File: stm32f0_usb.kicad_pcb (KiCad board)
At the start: 2 copper layers, 41 parts, among them J1 USB_B_Mini, J2 Conn_ARM_JTAG_SWD_10, J3 Conn_01x14_Male, J4 Conn_01x14_Male, SW1 B3S-1000P, SW2 B3S-1000P, U1 STM32F042K6Tx, U2 ADP121-AUJZ33R7, U3 USBLC6-2SC6, X1 ASV-8.000MHz

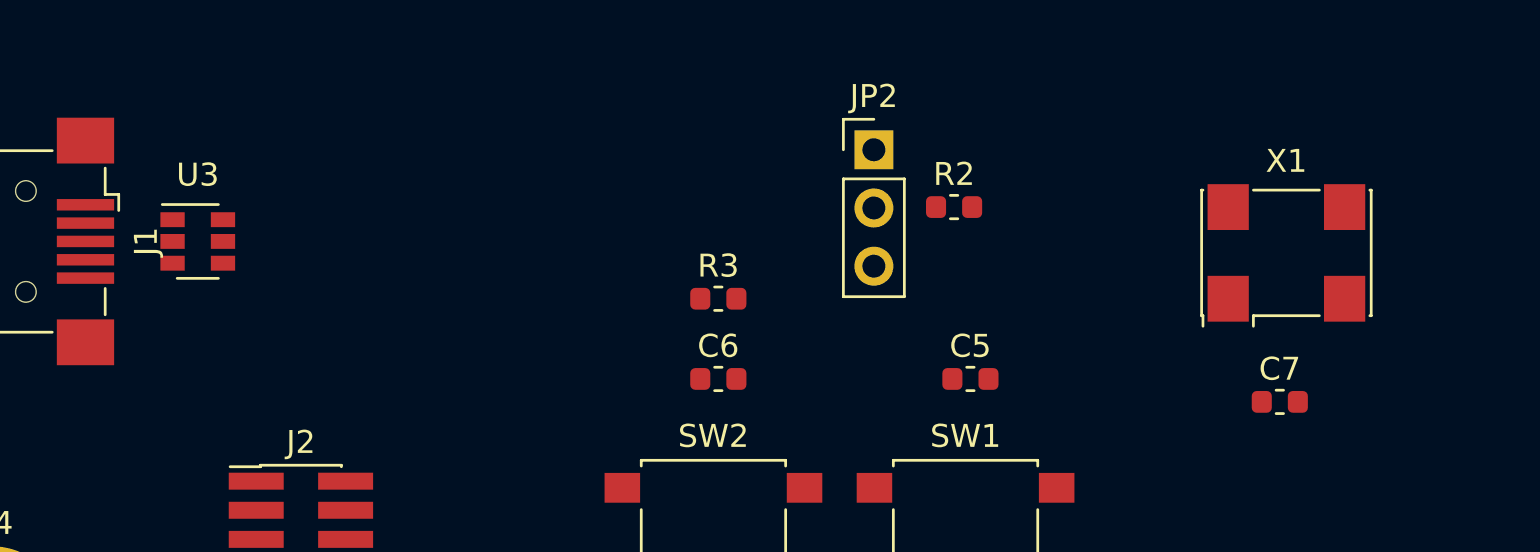
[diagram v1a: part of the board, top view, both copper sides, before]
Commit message: update usb esd connections
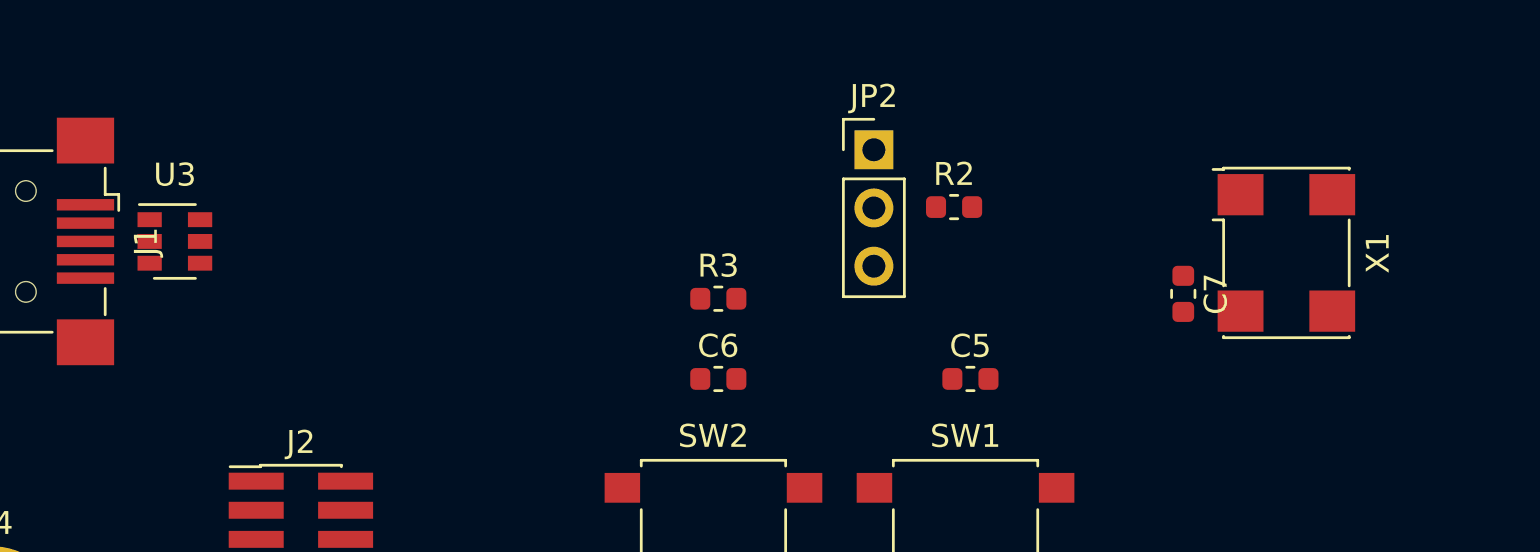
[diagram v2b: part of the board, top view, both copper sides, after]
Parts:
- moved C7 6.32 mm to (124.5, 94.8), turned to 270 degrees
- moved U3 1.00 mm to (80.5, 92.5)
- turned X1 to 270 degrees
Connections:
- D3 pad 2: /STM32/PA0 -> /STM32/PA1
- J3 pad 10: /STM32/PA7 -> /STM32/PA6
- J3 pad 11: /STM32/PA8 -> /STM32/PA7
- J3 pad 12: /STM32/PA9 -> /STM32/PB0
- J3 pad 13: /STM32/PA10 -> /STM32/PB1
- J3 pad 3: /STM32/PA0 -> /STM32/PF1
- J3 pad 4: /STM32/PA1 -> /STM32/PA0
- J3 pad 5: /STM32/PA2 -> /STM32/PA1
- J3 pad 6: /STM32/PA3 -> /STM32/PA2
- J3 pad 7: /STM32/PA4 -> /STM32/PA3
- J3 pad 8: /STM32/PA5 -> /STM32/PA4
- J3 pad 9: /STM32/PA6 -> /STM32/PA5
- J4 pad 10: /STM32/PB5 -> /STM32/PA13_SWDIO
- J4 pad 11: /STM32/PB6 -> /STM32/PA10
- J4 pad 12: /STM32/PB7 -> /STM32/PA9
- J4 pad 13: /STM32/PF1 -> /STM32/PA8
- J4 pad 3: /STM32/PA13_SWDIO -> /STM32/PB7
- J4 pad 4: /STM32/PA14_SWCLK -> /STM32/PB6
- J4 pad 5: /STM32/PA15 -> /STM32/PB5
- J4 pad 6: /STM32/PB0 -> /STM32/PB4
- J4 pad 7: /STM32/PB1 -> /STM32/PB3
- J4 pad 8: /STM32/PB3 -> /STM32/PA15
- J4 pad 9: /STM32/PB4 -> /STM32/PA14_SWCLK
- U3 pad 1: /STM32/USB_DM -> Net-(J1-Pad2)
- U3 pad 3: /STM32/USB_DP -> Net-(J1-Pad3)
- U3 pad 4: Net-(J1-Pad3) -> /STM32/USB_DP
- U3 pad 6: Net-(J1-Pad2) -> /STM32/USB_DM
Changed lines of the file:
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@@
   )
   (module Oscillator:Oscillator_SMD_Abracon_ASV-4Pin_7.0x5.1mm (layer F.Cu)
-    (at 129 93)
+    (at 129 93 270)
     (descr "Miniature Crystal Clock Oscillator Abracon ASV series, http://www.abracon.com/Oscillators/ASV.pdf, 7.0x5.1mm^2 package")
     (tags "SMD SMT crystal oscillator")
     (attr smd)
-    (fp_text reference X1 (at 0 -4) (layer F.SilkS)
-      (effects (font (size 1 1) (thickness 0.15)))
-    )
-    (fp_text value ASV-8.000MHz (at 0 4) (layer F.Fab)
+    (fp_text reference X1 (at 0 -4 90) (layer F.SilkS)
+      (effects (font (size 1 1) (thickness 0.15)))
+    )
+    (fp_text value ASV-8.000MHz (at 0 4 90) (layer F.Fab)
       (effects (font (size 1 1) (thickness 0.15)))
     )
@@
     (fp_line (start 3.4 -2.54) (end 3.5 -2.44) (layer F.Fab) (width 0.1))
     (fp_line (start -3.4 -2.54) (end 3.4 -2.54) (layer F.Fab) (width 0.1))
-    (fp_text user %R (at 0 0) (layer F.Fab)
-      (effects (font (size 1 1) (thickness 0.15)))
-    )
-    (pad 4 smd rect (at -2.54 -2) (size 1.8 2) (layers F.Cu F.Paste F.Mask)
+    (fp_text user %R (at 0 0 90) (layer F.Fab)
+      (effects (font (size 1 1) (thickness 0.15)))
+    )
+    (pad 4 smd rect (at -2.54 -2 270) (size 1.8 2) (layers F.Cu F.Paste F.Mask)
       (net 8 VDD))
-    (pad 3 smd rect (at 2.54 -2) (size 1.8 2) (layers F.Cu F.Paste F.Mask)
+    (pad 3 smd rect (at 2.54 -2 270) (size 1.8 2) (layers F.Cu F.Paste F.Mask)
       (net 47 /STM32/clkin))
-    (pad 2 smd rect (at 2.54 2) (size 1.8 2) (layers F.Cu F.Paste F.Mask)
-      (net 1 GND))
-    (pad 1 smd rect (at -2.54 2) (size 1.8 2) (layers F.Cu F.Paste F.Mask)
+    (pad 2 smd rect (at 2.54 2 270) (size 1.8 2) (layers F.Cu F.Paste F.Mask)
+      (net 1 GND))
+    (pad 1 smd rect (at -2.54 2 270) (size 1.8 2) (layers F.Cu F.Paste F.Mask)
       (net 46 "Net-(X1-Pad1)"))
     (model ${KISYS3DMOD}/Oscillator.3dshapes/Oscillator_SMD_Abracon_ASV-4Pin_7.0x5.1mm.wrl
@@
   )
   (module Package_TO_SOT_SMD:SOT-23-6 (layer F.Cu)
-    (at 81.5 92.5)
+    (at 80.5 92.5)
     (descr "6-pin SOT-23 package")
     (tags SOT-23-6)
@@
       (net 2 "Net-(C1-Pad1)"))
     (pad 6 smd rect (at 1.1 -0.95) (size 1.06 0.65) (layers F.Cu F.Paste F.Mask)
+      (net 44 /STM32/USB_DM))
+    (pad 4 smd rect (at 1.1 0.95) (size 1.06 0.65) (layers F.Cu F.Paste F.Mask)
+      (net 43 /STM32/USB_DP))
+    (pad 3 smd rect (at -1.1 0.95) (size 1.06 0.65) (layers F.Cu F.Paste F.Mask)
+      (net 15 "Net-(J1-Pad3)"))
+    (pad 2 smd rect (at -1.1 0) (size 1.06 0.65) (layers F.Cu F.Paste F.Mask)
+      (net 1 GND))
+    (pad 1 smd rect (at -1.1 -0.95) (size 1.06 0.65) (layers F.Cu F.Paste F.Mask)
       (net 16 "Net-(J1-Pad2)"))
-    (pad 4 smd rect (at 1.1 0.95) (size 1.06 0.65) (layers F.Cu F.Paste F.Mask)
-      (net 15 "Net-(J1-Pad3)"))
-    (pad 3 smd rect (at -1.1 0.95) (size 1.06 0.65) (layers F.Cu F.Paste F.Mask)
-      (net 43 /STM32/USB_DP))
-    (pad 2 smd rect (at -1.1 0) (size 1.06 0.65) (layers F.Cu F.Paste F.Mask)
-      (net 1 GND))
-    (pad 1 smd rect (at -1.1 -0.95) (size 1.06 0.65) (layers F.Cu F.Paste F.Mask)
-      (net 44 /STM32/USB_DM))
     (model ${KISYS3DMOD}/Package_TO_SOT_SMD.3dshapes/SOT-23-6.wrl
       (at (xyz 0 0 0))
@@
       (net 1 GND))
     (pad 13 thru_hole oval (at 0 30.48 90) (size 1.7 1.7) (drill 1) (layers *.Cu *.Mask)
-      (net 32 /STM32/PF1))
+      (net 24 /STM32/PA8))
     (pad 12 thru_hole oval (at 0 27.94 90) (size 1.7 1.7) (drill 1) (layers *.Cu *.Mask)
+      (net 23 /STM32/PA9))
+    (pad 11 thru_hole oval (at 0 25.4 90) (size 1.7 1.7) (drill 1) (layers *.Cu *.Mask)
+      (net 22 /STM32/PA10))
+    (pad 10 thru_hole oval (at 0 22.86 90) (size 1.7 1.7) (drill 1) (layers *.Cu *.Mask)
+      (net 21 /STM32/PA13_SWDIO))
+    (pad 9 thru_hole oval (at 0 20.32 90) (size 1.7 1.7) (drill 1) (layers *.Cu *.Mask)
+      (net 20 /STM32/PA14_SWCLK))
+    (pad 8 thru_hole oval (at 0 17.78 90) (size 1.7 1.7) (drill 1) (layers *.Cu *.Mask)
+      (net 40 /STM32/PA15))
+    (pad 7 thru_hole oval (at 0 15.24 90) (size 1.7 1.7) (drill 1) (layers *.Cu *.Mask)
+      (net 37 /STM32/PB3))
+    (pad 6 thru_hole oval (at 0 12.7 90) (size 1.7 1.7) (drill 1) (layers *.Cu *.Mask)
+      (net 36 /STM32/PB4))
+    (pad 5 thru_hole oval (at 0 10.16 90) (size 1.7 1.7) (drill 1) (layers *.Cu *.Mask)
+      (net 35 /STM32/PB5))
+    (pad 4 thru_hole oval (at 0 7.62 90) (size 1.7 1.7) (drill 1) (layers *.Cu *.Mask)
+      (net 34 /STM32/PB6))
+    (pad 3 thru_hole oval (at 0 5.08 90) (size 1.7 1.7) (drill 1) (layers *.Cu *.Mask)
       (net 33 /STM32/PB7))
-    (pad 11 thru_hole oval (at 0 25.4 90) (size 1.7 1.7) (drill 1) (layers *.Cu *.Mask)
-      (net 34 /STM32/PB6))
-    (pad 10 thru_hole oval (at 0 22.86 90) (size 1.7 1.7) (drill 1) (layers *.Cu *.Mask)
-      (net 35 /STM32/PB5))
-    (pad 9 thru_hole oval (at 0 20.32 90) (size 1.7 1.7) (drill 1) (layers *.Cu *.Mask)
-      (net 36 /STM32/PB4))
-    (pad 8 thru_hole oval (at 0 17.78 90) (size 1.7 1.7) (drill 1) (layers *.Cu *.Mask)
-      (net 37 /STM32/PB3))
-    (pad 7 thru_hole oval (at 0 15.24 90) (size 1.7 1.7) (drill 1) (layers *.Cu *.Mask)
-      (net 38 /STM32/PB1))
-    (pad 6 thru_hole oval (at 0 12.7 90) (size 1.7 1.7) (drill 1) (layers *.Cu *.Mask)
-      (net 39 /STM32/PB0))
-    (pad 5 thru_hole oval (at 0 10.16 90) (size 1.7 1.7) (drill 1) (layers *.Cu *.Mask)
-      (net 40 /STM32/PA15))
-    (pad 4 thru_hole oval (at 0 7.62 90) (size 1.7 1.7) (drill 1) (layers *.Cu *.Mask)
-      (net 20 /STM32/PA14_SWCLK))
-    (pad 3 thru_hole oval (at 0 5.08 90) (size 1.7 1.7) (drill 1) (layers *.Cu *.Mask)
-      (net 21 /STM32/PA13_SWDIO))
     (pad 2 thru_hole oval (at 0 2.54 90) (size 1.7 1.7) (drill 1) (layers *.Cu *.Mask)
       (net 1 GND))
@@
       (net 1 GND))
     (pad 13 thru_hole oval (at 0 30.48 90) (size 1.7 1.7) (drill 1) (layers *.Cu *.Mask)
-      (net 22 /STM32/PA10))
+      (net 38 /STM32/PB1))
     (pad 12 thru_hole oval (at 0 27.94 90) (size 1.7 1.7) (drill 1) (layers *.Cu *.Mask)
-      (net 23 /STM32/PA9))
+      (net 39 /STM32/PB0))
     (pad 11 thru_hole oval (at 0 25.4 90) (size 1.7 1.7) (drill 1) (layers *.Cu *.Mask)
-      (net 24 /STM32/PA8))
+      (net 25 /STM32/PA7))
     (pad 10 thru_hole oval (at 0 22.86 90) (size 1.7 1.7) (drill 1) (layers *.Cu *.Mask)
-      (net 25 /STM32/PA7))
+      (net 26 /STM32/PA6))
     (pad 9 thru_hole oval (at 0 20.32 90) (size 1.7 1.7) (drill 1) (layers *.Cu *.Mask)
-      (net 26 /STM32/PA6))
+      (net 27 /STM32/PA5))
     (pad 8 thru_hole oval (at 0 17.78 90) (size 1.7 1.7) (drill 1) (layers *.Cu *.Mask)
-      (net 27 /STM32/PA5))
+      (net 28 /STM32/PA4))
     (pad 7 thru_hole oval (at 0 15.24 90) (size 1.7 1.7) (drill 1) (layers *.Cu *.Mask)
-      (net 28 /STM32/PA4))
+      (net 29 /STM32/PA3))
     (pad 6 thru_hole oval (at 0 12.7 90) (size 1.7 1.7) (drill 1) (layers *.Cu *.Mask)
-      (net 29 /STM32/PA3))
+      (net 30 /STM32/PA2))
     (pad 5 thru_hole oval (at 0 10.16 90) (size 1.7 1.7) (drill 1) (layers *.Cu *.Mask)
-      (net 30 /STM32/PA2))
+      (net 31 /STM32/PA1))
     (pad 4 thru_hole oval (at 0 7.62 90) (size 1.7 1.7) (drill 1) (layers *.Cu *.Mask)
-      (net 31 /STM32/PA1))
+      (net 11 /STM32/PA0))
     (pad 3 thru_hole oval (at 0 5.08 90) (size 1.7 1.7) (drill 1) (layers *.Cu *.Mask)
-      (net 11 /STM32/PA0))
+      (net 32 /STM32/PF1))
     (pad 2 thru_hole oval (at 0 2.54 90) (size 1.7 1.7) (drill 1) (layers *.Cu *.Mask)
       (net 1 GND))
@@
     (fp_line (start 0.8 -0.4) (end -0.5 -0.4) (layer F.Fab) (width 0.1))
     (pad 2 smd roundrect (at 0.8125 0) (size 1.225 0.85) (layers F.Cu F.Paste F.Mask) (roundrect_rratio 0.25)
-      (net 11 /STM32/PA0))
+      (net 31 /STM32/PA1))
     (pad 1 smd roundrect (at -0.8125 0) (size 1.225 0.85) (layers F.Cu F.Paste F.Mask) (roundrect_rratio 0.25)
       (net 13 "Net-(D3-Pad1)"))
@@
   )
   (module Capacitor_SMD:C_0603_1608Metric (layer F.Cu)
-    (at 128.7125 99.5)
+    (at 124.5 94.7875 270)
     (descr "Capacitor SMD 0603 (1608 Metric), square (rectangular) end terminal, IPC_7351 nominal, (Body size source: http://www.tortai-tech.com/upload/download/2011102023233369053.pdf), generated with kicad-footprint-generator")
     (tags capacitor)
     (attr smd)
-    (fp_text reference C7 (at 0 -1.43) (layer F.SilkS)
-      (effects (font (size 1 1) (thickness 0.15)))
-    )
-    (fp_text value 10n (at 0 1.43) (layer F.Fab)
-      (effects (font (size 1 1) (thickness 0.15)))
-    )
-    (fp_text user %R (at 0 0) (layer F.Fab)
+    (fp_text reference C7 (at 0 -1.43 90) (layer F.SilkS)
+      (effects (font (size 1 1) (thickness 0.15)))
+    )
+    (fp_text value 10n (at 0 1.43 90) (layer F.Fab)
+      (effects (font (size 1 1) (thickness 0.15)))
+    )
+    (fp_text user %R (at 0 0 90) (layer F.Fab)
       (effects (font (size 0.4 0.4) (thickness 0.06)))
     )
@@
     (fp_line (start -0.8 -0.4) (end 0.8 -0.4) (layer F.Fab) (width 0.1))
     (fp_line (start -0.8 0.4) (end -0.8 -0.4) (layer F.Fab) (width 0.1))
-    (pad 2 smd roundrect (at 0.7875 0) (size 0.875 0.95) (layers F.Cu F.Paste F.Mask) (roundrect_rratio 0.25)
-      (net 1 GND))
-    (pad 1 smd roundrect (at -0.7875 0) (size 0.875 0.95) (layers F.Cu F.Paste F.Mask) (roundrect_rratio 0.25)
+    (pad 2 smd roundrect (at 0.7875 0 270) (size 0.875 0.95) (layers F.Cu F.Paste F.Mask) (roundrect_rratio 0.25)
+      (net 1 GND))
+    (pad 1 smd roundrect (at -0.7875 0 270) (size 0.875 0.95) (layers F.Cu F.Paste F.Mask) (roundrect_rratio 0.25)
       (net 8 VDD))
     (model ${KISYS3DMOD}/Capacitor_SMD.3dshapes/C_0603_1608Metric.wrl

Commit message: initial routing mostly finished
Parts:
- NT1: footprint NetTie:NetTie-2_THT_Pad1.0mm -> NetTie:NetTie-2_SMD_Pad0.5mm
- moved H2 135.4 mm to (105.0, 105.0)
- moved H1 96.0 mm to (165.0, 105.0)
- moved C1 65.1 mm to (116.0, 115.0)
- moved FB1 64.2 mm to (118.2, 114.2)
- moved C2 61.8 mm to (118.2, 115.8), turned to 180 degrees
- moved SW2 61.3 mm to (164.0, 118.0), turned to 270 degrees
- moved R3 59.3 mm to (159.0, 117.7), turned to 270 degrees
- moved D2 57.2 mm to (163.0, 135.0), turned to 270 degrees
- moved C6 57.1 mm to (159.0, 114.8), turned to 90 degrees
- moved NT1 56.3 mm to (130.0, 135.0)
- moved D4 56.1 mm to (120.5, 111.5)
- moved R4 55.1 mm to (163.0, 131.5), turned to 90 degrees
- moved C12 54.7 mm to (137.2, 125.0), turned to 90 degrees
- moved C9 52.4 mm to (136.9, 133.0)
- moved U2 52.0 mm to (126.5, 111.5)
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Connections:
- net Net-(C1-Pad1) renamed VBUS
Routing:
- net /STM32/USB_DP: track 0.00 -> 83.3 mm
- net /STM32/USB_DM: track 0.00 -> 78.7 mm
- net VDD: track 0.00 -> 72.3 mm
- net /STM32/PA2: track 0.00 -> 72.2 mm
- net /STM32/PA0: track 0.00 -> 66.5 mm
- net GND: track 0.00 -> 65.3 mm, vias 0 -> 21
- net /STM32/PA1: track 0.00 -> 61.2 mm
- net /STM32/NRST: track 0.00 -> 53.3 mm, vias 0 -> 2
- net /STM32/PF1: track 0.00 -> 43.2 mm, vias 0 -> 2
- net /STM32/BOOT0: track 0.00 -> 24.2 mm
- net /STM32/PB7: track 0.00 -> 23.7 mm
- net /STM32/PB6: track 0.00 -> 22.4 mm
- net /STM32/PB5: track 0.00 -> 21.0 mm
- net /STM32/PB1: track 0.00 -> 19.8 mm
- net /STM32/PA4: track 0.00 -> 19.6 mm
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- added copper zone on B.Cu, net GND
- added copper zone on F.Cu, net VDD
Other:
- board outline added: 70 x 50 mm
- net class usb: clearance 0.4 -> 0.2; trace_width 0.4064 -> 0.3048
- board text added: "TODO move USB connector? redo vdd-vdda routing move BOOT0 jumper"
